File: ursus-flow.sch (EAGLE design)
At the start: 62 parts

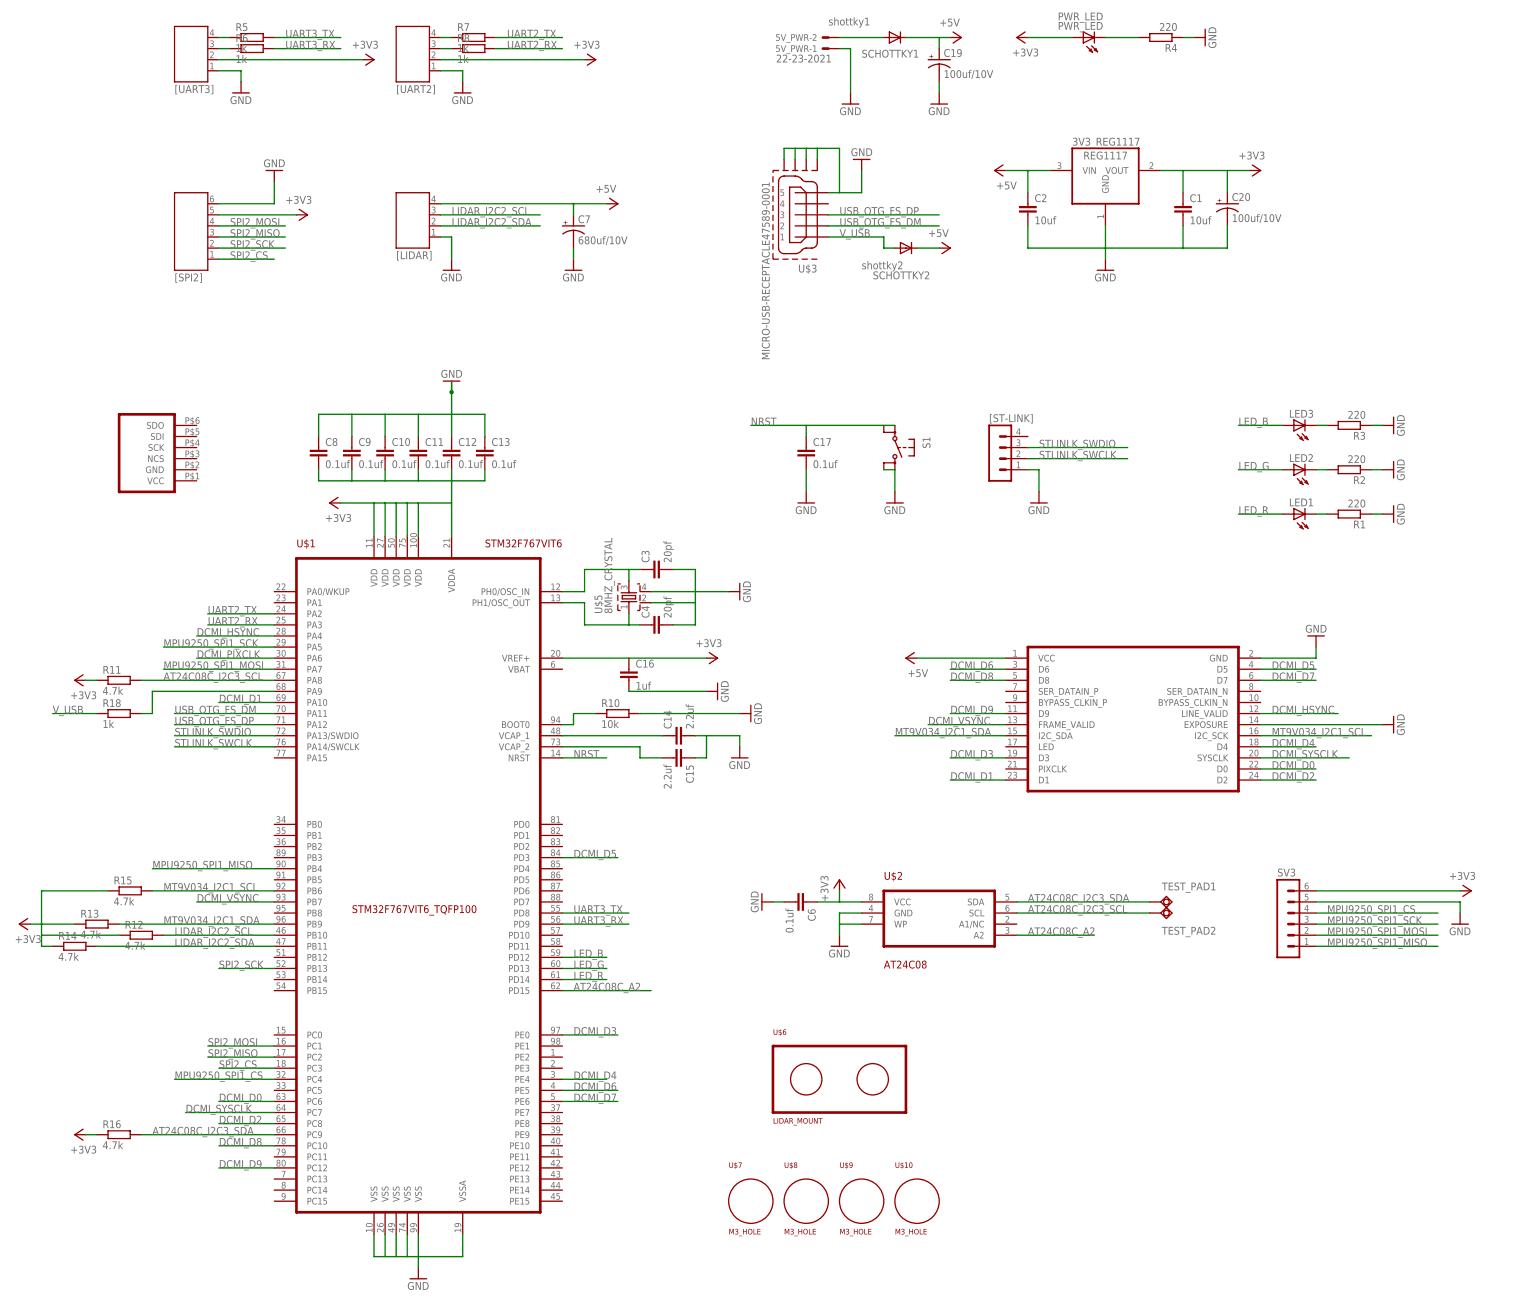
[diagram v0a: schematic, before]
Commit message: Remove wrong footprint of MPU9250
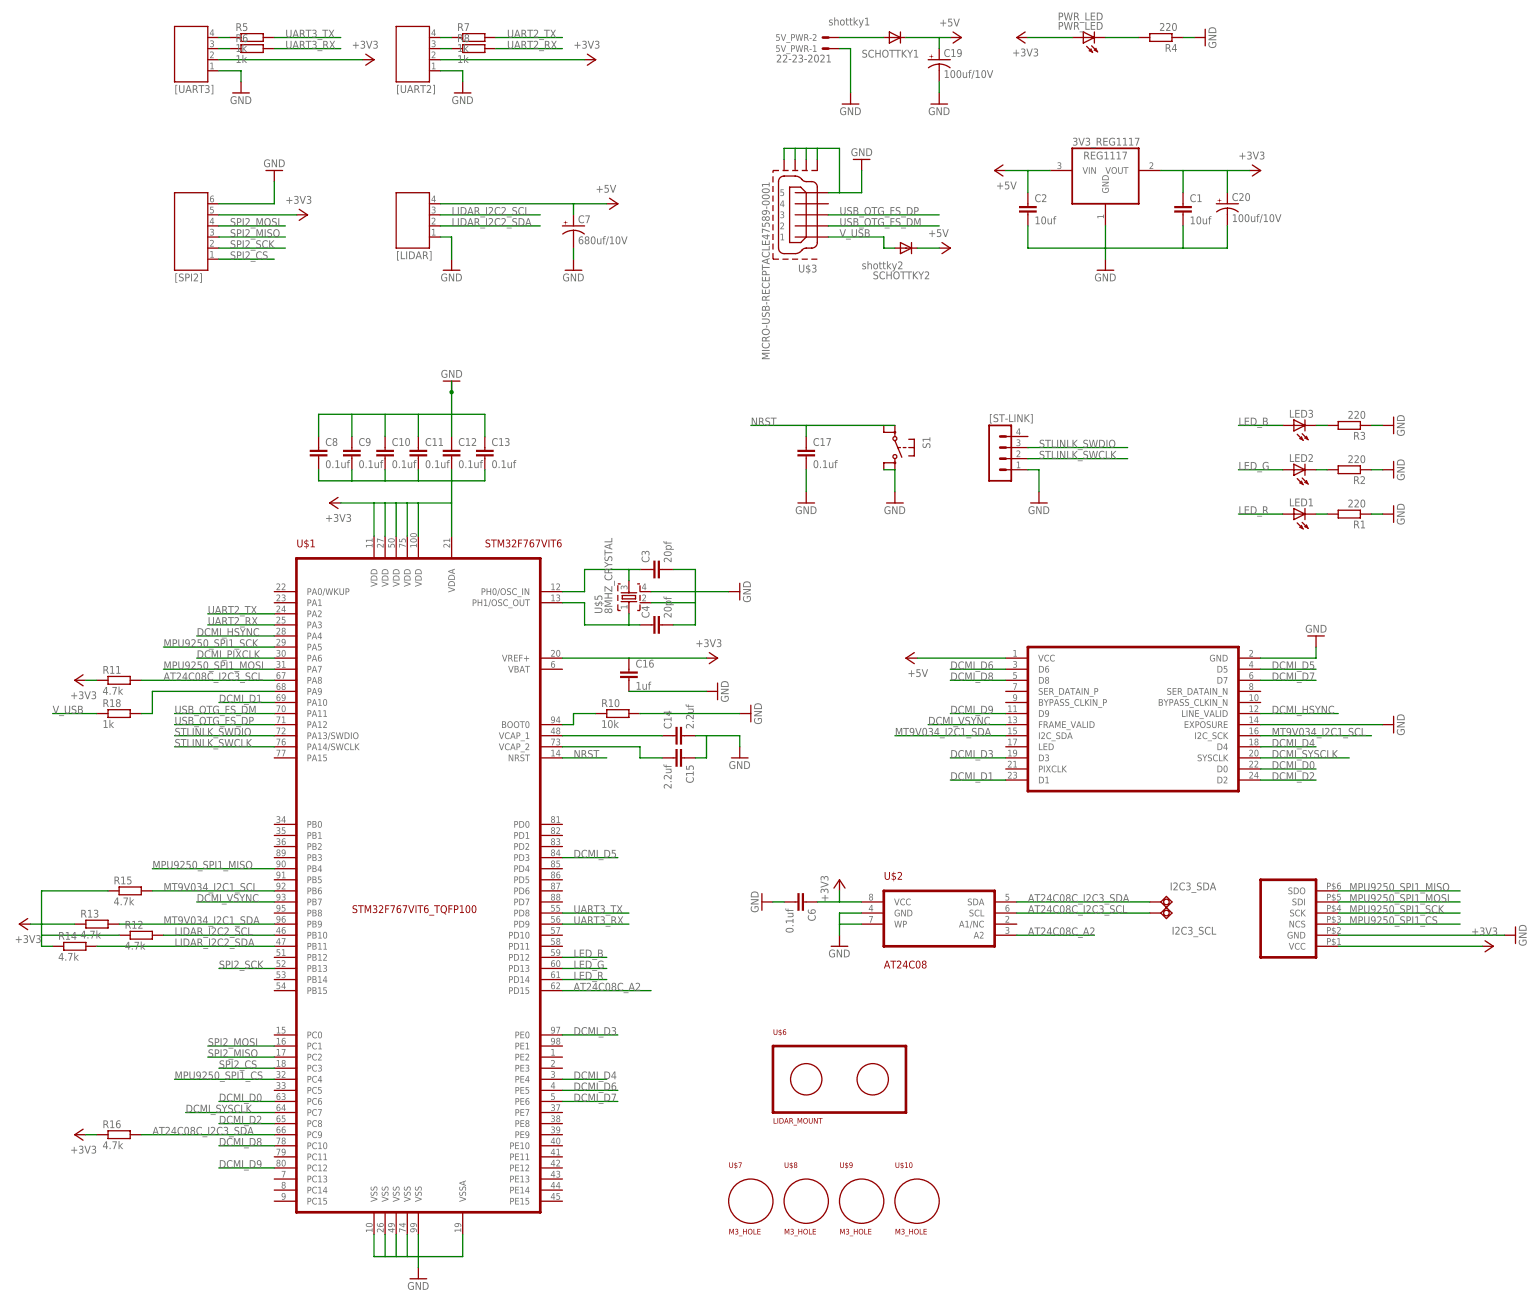
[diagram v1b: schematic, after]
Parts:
- removed SV3: (no value), con-lstb:MA06-1
- renumbered TEST_PAD1 to I2C3_SDA, TEST_PAD2 to I2C3_SCL
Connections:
- net +3V3: now also U$11.VCC; no longer SV3.6
- net GND: now also U$11.GND; no longer SV3.5
- net MPU9250_SPI1_CS: now also U$11.NCS; no longer SV3.4
- net MPU9250_SPI1_MISO: now also U$11.SDO; no longer SV3.1
- net MPU9250_SPI1_MOSI: now also U$11.SDI; no longer SV3.2
- net MPU9250_SPI1_SCK: now also U$11.SCK; no longer SV3.3
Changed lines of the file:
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@@
 <part name="C13" library="rcl" deviceset="C-EU" device="C0805" value="0.1uf"/>
 <part name="GND19" library="supply1" deviceset="GND" device=""/>
-<part name="+3V7" library="supply1" deviceset="+3V3" device=""/>
-<part name="GND20" library="supply1" deviceset="GND" device=""/>
-<part name="SV3" library="con-lstb" deviceset="MA06-1" device=""/>
 <part name="R5" library="rcl" deviceset="R-EU_" device="M0805" value="1k"/>
 <part name="R6" library="rcl" deviceset="R-EU_" device="M0805" value="1k"/>
@@
 <part name="SCHOTTKY2" library="_mod_diode" deviceset="DIODE-" device="SOD323-W" value="shottky2"/>
 <part name="SCHOTTKY1" library="_mod_diode" deviceset="DIODE-" device="SOD323-W" value="shottky1"/>
-<part name="TEST_PAD1" library="testpad" deviceset="TPSQ" device="TP20SQ"/>
-<part name="TEST_PAD2" library="testpad" deviceset="TPSQ" device="TP20SQ"/>
+<part name="I2C3_SDA" library="testpad" deviceset="TPSQ" device="TP20SQ"/>
+<part name="I2C3_SCL" library="testpad" deviceset="TPSQ" device="TP20SQ"/>
 <part name="U$6" library="LIDAR_MOUNT" deviceset="LIDAR_MOUNT" device=""/>
 <part name="U$7" library="M3_HOLE" deviceset="M3_HOLE" device=""/>
@@
 <part name="U$10" library="M3_HOLE" deviceset="M3_HOLE" device=""/>
 <part name="U$11" library="MPU9250_BREAKOUT" deviceset="MPU9250_BREAKOUT" device=""/>
+<part name="+3V9" library="supply1" deviceset="+3V3" device=""/>
+<part name="GND8" library="supply1" deviceset="GND" device=""/>
 </parts>
 <sheets>
@@
 <text x="-76.2" y="213.36" size="1.778" layer="98">UART2</text>
 <text x="-76.2" y="175.26" size="1.778" layer="98">Lidar</text>
-<text x="124.46" y="20.32" size="1.778" layer="98">MPU9250(Breakboard Module)</text>
+<text x="121.92" y="17.78" size="1.778" layer="98">MPU9250(Breakboard Module)</text>
 <text x="68.58" y="71.12" size="1.778" layer="98">MT9V034(Breakboard Module)</text>
 <text x="10.16" y="213.36" size="1.778" layer="98">Power from UBEC (5V)</text>
@@
 <instance part="C13" gate="G$1" x="-55.88" y="114.3"/>
 <instance part="GND19" gate="1" x="-63.5" y="129.54" rot="R180"/>
-<instance part="+3V7" gate="G$1" x="170.18" y="12.7" rot="R270"/>
-<instance part="GND20" gate="1" x="167.64" y="5.08"/>
-<instance part="SV3" gate="1" x="127" y="7.62"/>
 <instance part="R5" gate="G$1" x="-109.22" y="208.28"/>
 <instance part="R6" gate="G$1" x="-109.22" y="205.74"/>
@@
 <attribute name="VALUE" x="22.86" y="211.0486" size="1.778" layer="96"/>
 </instance>
-<instance part="TEST_PAD1" gate="G$1" x="99.06" y="10.16" smashed="yes" rot="R90">
+<instance part="I2C3_SDA" gate="G$1" x="99.06" y="10.16" smashed="yes" rot="R90">
 <attribute name="NAME" x="111.76" y="14.605" size="1.778" layer="95" rot="R180"/>
 <attribute name="TP_SIGNAL_NAME" x="100.33" y="12.7" size="1.778" layer="97" rot="R90"/>
 </instance>
-<instance part="TEST_PAD2" gate="G$1" x="99.06" y="7.62" smashed="yes" rot="R90">
+<instance part="I2C3_SCL" gate="G$1" x="99.06" y="7.62" smashed="yes" rot="R90">
 <attribute name="NAME" x="111.76" y="4.445" size="1.778" layer="95" rot="R180"/>
 <attribute name="TP_SIGNAL_NAME" x="100.33" y="10.16" size="1.778" layer="97" rot="R90"/>
@@
 <instance part="U$9" gate="G$1" x="30.48" y="-58.42"/>
 <instance part="U$10" gate="G$1" x="43.18" y="-58.42"/>
-<instance part="U$11" gate="G$1" x="-132.08" y="116.84" rot="R180"/>
+<instance part="U$11" gate="G$1" x="129.54" y="10.16" rot="R180"/>
+<instance part="+3V9" gate="G$1" x="175.26" y="0" rot="R270"/>
+<instance part="GND8" gate="1" x="180.34" y="2.54" rot="R90"/>
 </instances>
 <busses>
@@
 </segment>
 <segment>
-<pinref part="SV3" gate="1" pin="5"/>
-<wire x1="134.62" y1="10.16" x2="167.64" y2="10.16" width="0.1524" layer="91"/>
-<pinref part="GND20" gate="1" pin="GND"/>
-<wire x1="167.64" y1="10.16" x2="167.64" y2="7.62" width="0.1524" layer="91"/>
-</segment>
-<segment>
 <pinref part="C14" gate="G$1" pin="2"/>
 <wire x1="-7.62" y1="48.26" x2="-5.08" y2="48.26" width="0.1524" layer="91"/>
@@
 <pinref part="C19" gate="G$1" pin="-"/>
 <wire x1="48.26" y1="195.58" x2="48.26" y2="198.12" width="0.1524" layer="91"/>
+</segment>
+<segment>
+<wire x1="139.7" y1="2.54" x2="177.8" y2="2.54" width="0.1524" layer="91"/>
+<pinref part="GND8" gate="1" pin="GND"/>
+<pinref part="U$11" gate="G$1" pin="GND"/>
 </segment>
 </net>
@@
 </segment>
 <segment>
-<pinref part="SV3" gate="1" pin="6"/>
-<pinref part="+3V7" gate="G$1" pin="+3V3"/>
-<wire x1="134.62" y1="12.7" x2="167.64" y2="12.7" width="0.1524" layer="91"/>
-</segment>
-<segment>
 <pinref part="U$1" gate="G$1" pin="VREF+"/>
 <pinref part="C16" gate="G$1" pin="1"/>
@@
 <wire x1="-147.32" y1="60.96" x2="-144.78" y2="60.96" width="0.1524" layer="91"/>
 </segment>
+<segment>
+<wire x1="139.7" y1="0" x2="172.72" y2="0" width="0.1524" layer="91"/>
+<pinref part="+3V9" gate="G$1" pin="+3V3"/>
+<pinref part="U$11" gate="G$1" pin="VCC"/>
+</segment>
 </net>
 <net name="USB_OTG_FS_DP" class="0">
@@
 </segment>
 <segment>
-<wire x1="162.56" y1="5.08" x2="134.62" y2="5.08" width="0.1524" layer="91"/>
-<label x="137.16" y="5.08" size="1.778" layer="95"/>
-<pinref part="SV3" gate="1" pin="3"/>
+<wire x1="167.64" y1="7.62" x2="139.7" y2="7.62" width="0.1524" layer="91"/>
+<label x="142.24" y="7.62" size="1.778" layer="95"/>
+<pinref part="U$11" gate="G$1" pin="SCK"/>
 </segment>
 </net>
@@
 </segment>
 <segment>
-<wire x1="162.56" y1="2.54" x2="134.62" y2="2.54" width="0.1524" layer="91"/>
-<label x="137.16" y="2.54" size="1.778" layer="95"/>
-<pinref part="SV3" gate="1" pin="2"/>
+<wire x1="167.64" y1="10.16" x2="139.7" y2="10.16" width="0.1524" layer="91"/>
+<label x="142.24" y="10.16" size="1.778" layer="95"/>
+<pinref part="U$11" gate="G$1" pin="SDI"/>
 </segment>
 </net>
@@
 </segment>
 <segment>
-<wire x1="162.56" y1="0" x2="134.62" y2="0" width="0.1524" layer="91"/>
-<label x="137.16" y="0" size="1.778" layer="95"/>
-<pinref part="SV3" gate="1" pin="1"/>
+<wire x1="167.64" y1="12.7" x2="139.7" y2="12.7" width="0.1524" layer="91"/>
+<label x="142.24" y="12.7" size="1.778" layer="95"/>
+<pinref part="U$11" gate="G$1" pin="SDO"/>
 </segment>
 </net>
@@
 <label x="68.58" y="7.62" size="1.778" layer="95"/>
 <pinref part="U$2" gate="G$1" pin="SCL"/>
-<pinref part="TEST_PAD2" gate="G$1" pin="TP"/>
+<pinref part="I2C3_SCL" gate="G$1" pin="TP"/>
 </segment>
 </net>
@@
 <label x="68.58" y="10.16" size="1.778" layer="95"/>
 <pinref part="U$2" gate="G$1" pin="SDA"/>
-<pinref part="TEST_PAD1" gate="G$1" pin="TP"/>
+<pinref part="I2C3_SDA" gate="G$1" pin="TP"/>
 </segment>
 </net>
@@
 </segment>
 <segment>
-<wire x1="162.56" y1="7.62" x2="134.62" y2="7.62" width="0.1524" layer="91"/>
-<label x="137.16" y="7.62" size="1.778" layer="95"/>
-<pinref part="SV3" gate="1" pin="4"/>
-</segment>
-</net>
+<wire x1="167.64" y1="5.08" x2="139.7" y2="5.08" width="0.1524" layer="91"/>
+<label x="142.24" y="5.08" size="1.778" layer="95"/>
+<pinref part="U$11" gate="G$1" pin="NCS"/>
+</segment>
+</net>

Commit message: Start doing PCB layout
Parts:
- LED1: value (none) -> R
- LED2: value (none) -> G
- LED3: value (none) -> B
- [LIDAR]: value (none) -> lidar_connector
- [SPI2]: value (none) -> spi2_connector
- [ST-LINK]: value (none) -> stlink_connector
- [UART2]: value (none) -> uart2_connector
- [UART3]: value (none) -> uart3_connector
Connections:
- removed net N$16: C17.1, S1.P, S1.P1
- removed net N$5: C10.1, C11.1, C12.1, C13.1, C8.1, C9.1
- net AT24C08C_A2: now also U$1.PD15
- net DCMI_D3: now also U$1.PE1; no longer U$1.PE0
- net DCMI_PIXCLK: now also U$4.PIXCLK
- net GND: now also C10.1, C11.1, C12.1, C13.1, C8.1, C9.1
- net NRST: now also C17.1, S1.P, S1.P1
- net UART2_RX: now also R8.2
- net UART2_TX: now also R7.2
- net UART3_RX: now also R6.2
- net V_USB: now also R18.1
